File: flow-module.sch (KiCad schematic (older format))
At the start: 13 parts

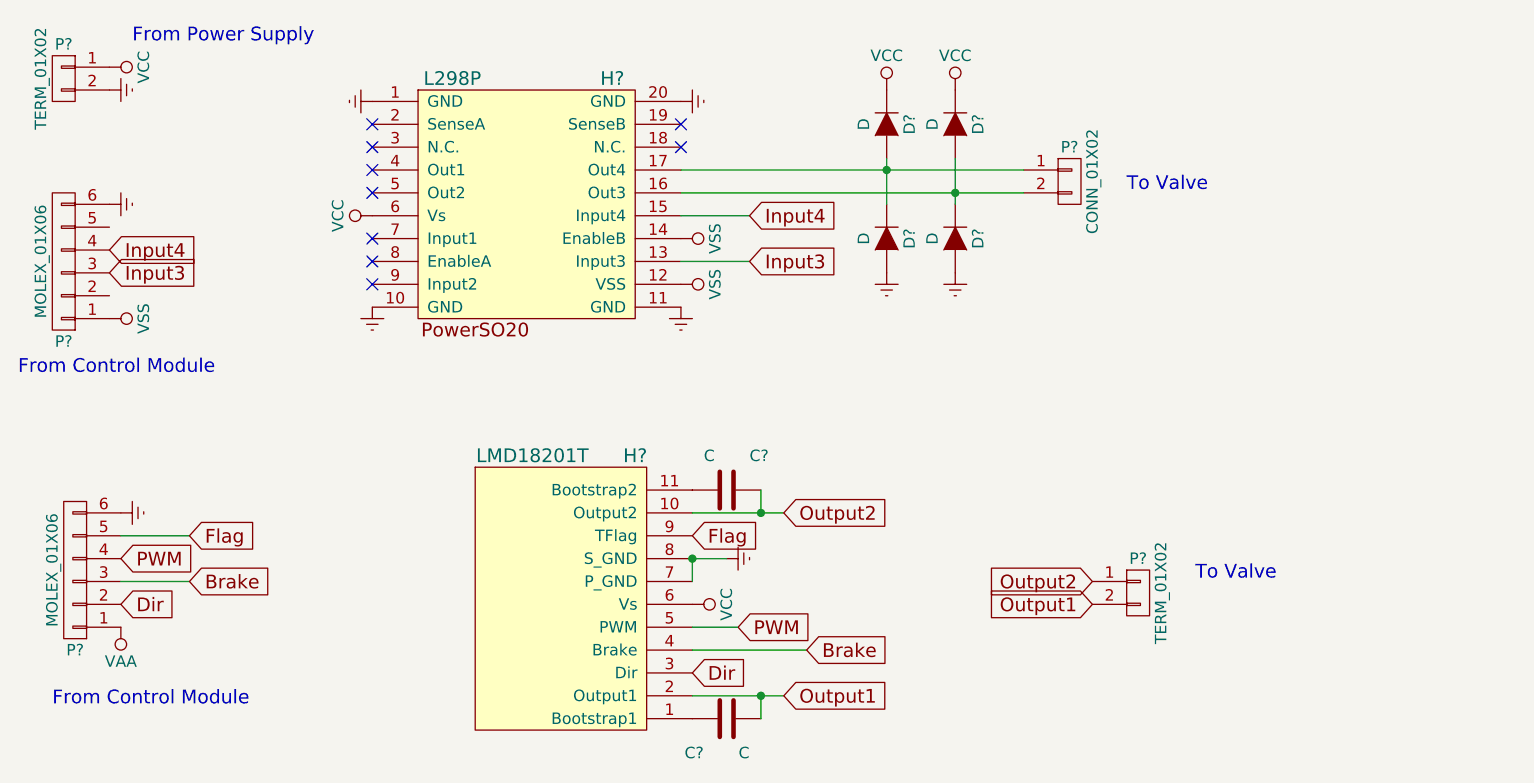
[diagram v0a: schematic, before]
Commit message: Added status LEDs to the schematic.
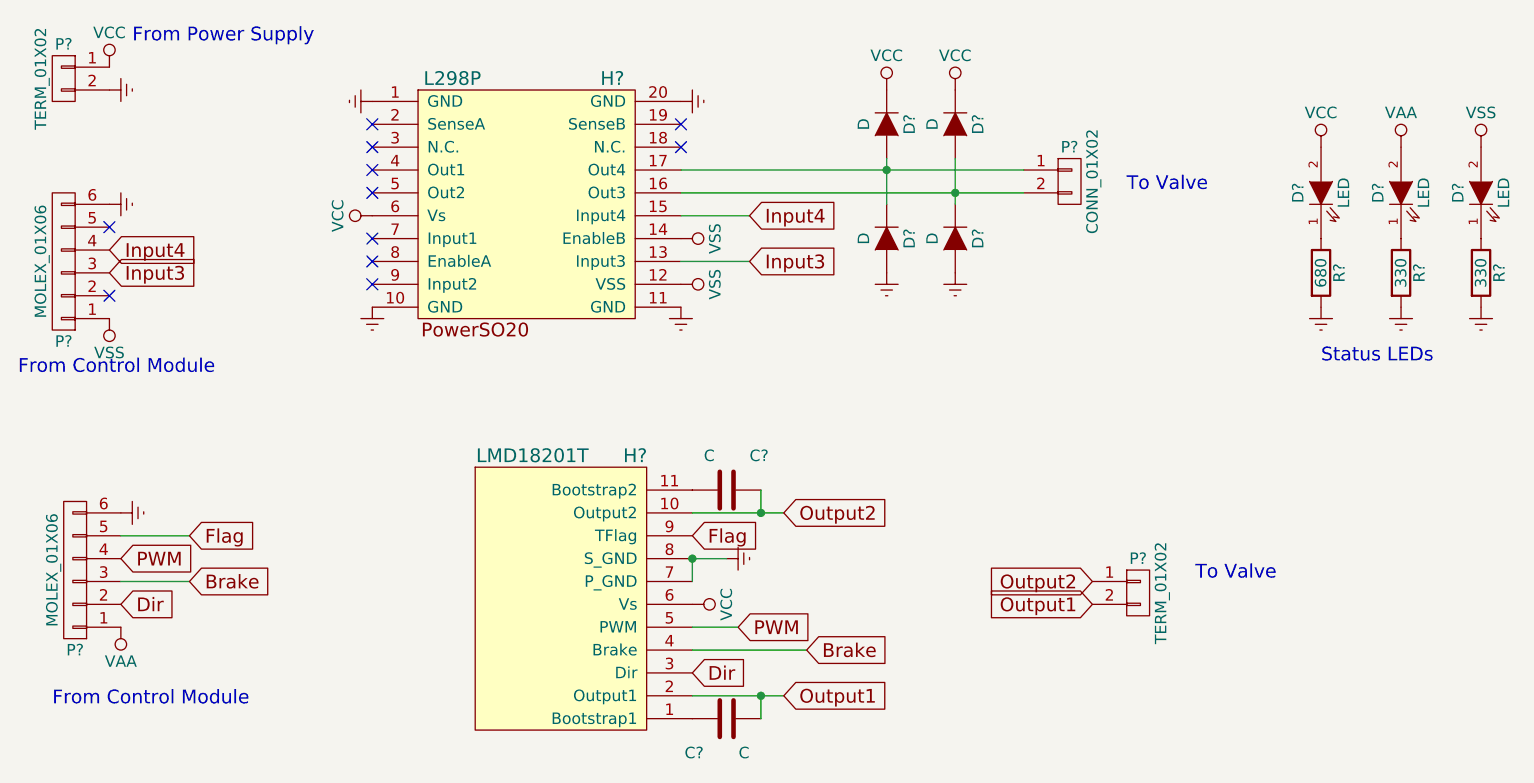
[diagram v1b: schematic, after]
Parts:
- added D? (x3): LED, symbol LED
- added R?: 680, symbol R
- added R? (x2): 330, symbol R
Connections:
- net Earth: now also R?.2, R?.2, R?.2
- net VAA: now also D?.2 (A)
- net VCC: now also D?.2 (A)
- net VSS: now also D?.2 (A)
- new net: D?.1 (K), R?.1 (x3)
- no-connect marks 9 -> 11
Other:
- note added: "Status LEDs\n"
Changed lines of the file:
@@
 LIBS:valves
 LIBS:valveteam
+LIBS:flow-module-cache
 EELAYER 25 0
 EELAYER END
@@
 F 3 "" H 1150 800 50  0000 C CNN
 	1    1150 800
-	0    1    1    0
+	1    0    0    -1
 $EndComp
 $Comp
@@
 F 3 "" H 1150 1900 50  0000 C CNN
 	1    1150 1900
-	0    1    1    0
+	-1   0    0    1
 $EndComp
 $Comp
@@
 Text Notes 900  3600 0    60   ~ 0
 From Control Module\n
+$Comp
+L VCC #PWR?
+U 1 1 5B052ACC
+P 6450 1150
+F 0 "#PWR?" H 6450 1000 50  0001 C CNN
+F 1 "VCC" H 6450 1300 50  0000 C CNN
+F 2 "" H 6450 1150 50  0000 C CNN
+F 3 "" H 6450 1150 50  0000 C CNN
+	1    6450 1150
+	1    0    0    -1
+$EndComp
+$Comp
+L VAA #PWR?
+U 1 1 5B052B8B
+P 6800 1150
+F 0 "#PWR?" H 6800 1000 50  0001 C CNN
+F 1 "VAA" H 6800 1300 50  0000 C CNN
+F 2 "" H 6800 1150 50  0000 C CNN
+F 3 "" H 6800 1150 50  0000 C CNN
+	1    6800 1150
+	1    0    0    -1
+$EndComp
+$Comp
+L VSS #PWR?
+U 1 1 5B052BBD
+P 7150 1150
+F 0 "#PWR?" H 7150 1000 50  0001 C CNN
+F 1 "VSS" H 7150 1300 50  0000 C CNN
+F 2 "" H 7150 1150 50  0000 C CNN
+F 3 "" H 7150 1150 50  0000 C CNN
+	1    7150 1150
+	1    0    0    -1
+$EndComp
+$Comp
+L LED D?
+U 1 1 5B052BE4
+P 6450 1350
+F 0 "D?" H 6450 1450 50  0000 C CNN
+F 1 "LED" H 6450 1250 50  0000 C CNN
+F 2 "" H 6450 1350 50  0000 C CNN
+F 3 "" H 6450 1350 50  0000 C CNN
+	1    6450 1350
+	0    -1   -1   0
+$EndComp
+$Comp
+L LED D?
+U 1 1 5B052C8D
+P 6800 1350
+F 0 "D?" H 6800 1450 50  0000 C CNN
+F 1 "LED" H 6800 1250 50  0000 C CNN
+F 2 "" H 6800 1350 50  0000 C CNN
+F 3 "" H 6800 1350 50  0000 C CNN
+	1    6800 1350
+	0    -1   -1   0
+$EndComp
+$Comp
+L LED D?
+U 1 1 5B052CD0
+P 7150 1350
+F 0 "D?" H 7150 1450 50  0000 C CNN
+F 1 "LED" H 7150 1250 50  0000 C CNN
+F 2 "" H 7150 1350 50  0000 C CNN
+F 3 "" H 7150 1350 50  0000 C CNN
+	1    7150 1350
+	0    -1   -1   0
+$EndComp
+$Comp
+L R R?
+U 1 1 5B052D3E
+P 6450 1700
+F 0 "R?" V 6530 1700 50  0000 C CNN
+F 1 "680" V 6450 1700 50  0000 C CNN
+F 2 "" V 6380 1700 50  0000 C CNN
+F 3 "" H 6450 1700 50  0000 C CNN
+	1    6450 1700
+	1    0    0    -1
+$EndComp
+$Comp
+L R R?
+U 1 1 5B052DC4
+P 6800 1700
+F 0 "R?" V 6880 1700 50  0000 C CNN
+F 1 "330" V 6800 1700 50  0000 C CNN
+F 2 "" V 6730 1700 50  0000 C CNN
+F 3 "" H 6800 1700 50  0000 C CNN
+	1    6800 1700
+	1    0    0    -1
+$EndComp
+$Comp
+L R R?
+U 1 1 5B052E1E
+P 7150 1700
+F 0 "R?" V 7230 1700 50  0000 C CNN
+F 1 "330" V 7150 1700 50  0000 C CNN
+F 2 "" V 7080 1700 50  0000 C CNN
+F 3 "" H 7150 1700 50  0000 C CNN
+	1    7150 1700
+	1    0    0    -1
+$EndComp
+$Comp
+L Earth #PWR?
+U 1 1 5B052E71
+P 6450 1850
+F 0 "#PWR?" H 6450 1600 50  0001 C CNN
+F 1 "Earth" H 6450 1700 50  0001 C CNN
+F 2 "" H 6450 1850 50  0000 C CNN
+F 3 "" H 6450 1850 50  0000 C CNN
+	1    6450 1850
+	1    0    0    -1
+$EndComp
+$Comp
+L Earth #PWR?
+U 1 1 5B052EB5
+P 6800 1850
+F 0 "#PWR?" H 6800 1600 50  0001 C CNN
+F 1 "Earth" H 6800 1700 50  0001 C CNN
+F 2 "" H 6800 1850 50  0000 C CNN
+F 3 "" H 6800 1850 50  0000 C CNN
+	1    6800 1850
+	1    0    0    -1
+$EndComp
+$Comp
+L Earth #PWR?
+U 1 1 5B052EF9
+P 7150 1850
+F 0 "#PWR?" H 7150 1600 50  0001 C CNN
+F 1 "Earth" H 7150 1700 50  0001 C CNN
+F 2 "" H 7150 1850 50  0000 C CNN
+F 3 "" H 7150 1850 50  0000 C CNN
+	1    7150 1850
+	1    0    0    -1
+$EndComp
+Text Notes 6450 2100 0    60   ~ 0
+Status LEDs\n
+NoConn ~ 1150 1500
+NoConn ~ 1150 1800
 $EndSCHEMATC

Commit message: Associate components and update the netlist.
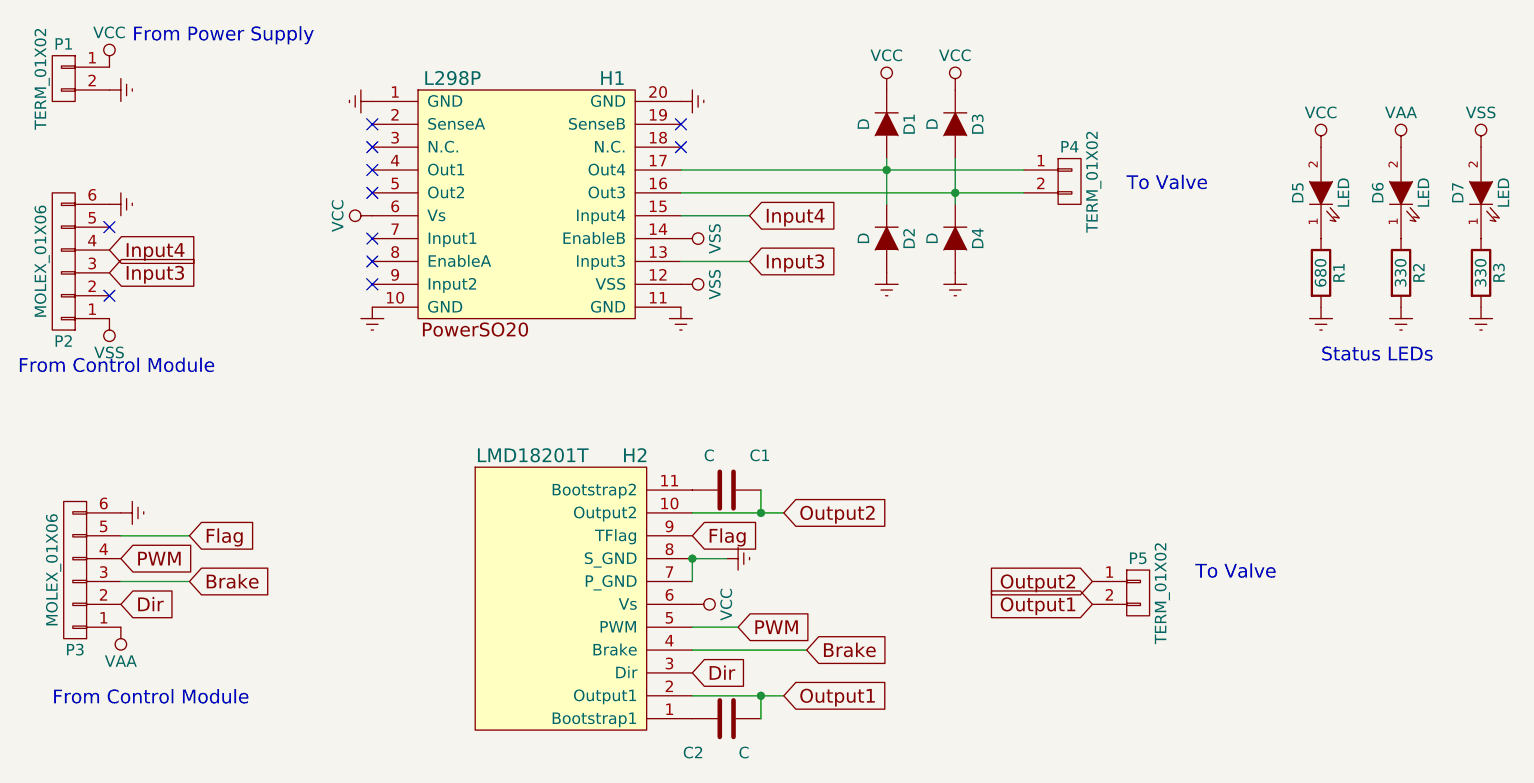
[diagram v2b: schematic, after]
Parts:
- removed P?: CONN_01X02, symbol CONN_01X02
- added P4: TERM_01X02, ValveTeam:TE_TERM, symbol CONN_01X02
- C1, C2: renamed from C?; footprint (none) -> Capacitors_SMD:C_0805_HandSoldering
- D1, D2, D3, D4: renamed from D?; footprint (none) -> ValveTeam:do219ab
- D5, D6, D7: renamed from D?; footprint (none) -> LEDs:LED_0805_HandSoldering
- H1: renamed from H?; footprint (none) -> ValveTeam:powerso-20
- H2: renamed from H?; footprint (none) -> ValveTeam:TO-220-11
- P1, P5: renamed from P?; footprint (none) -> ValveTeam:TE_TERM
- P2, P3: renamed from P?; footprint (none) -> ValveTeam:Molex_KK-6410-06_06x2.54mm_Straight
- R1, R2, R3: renamed from R?; footprint (none) -> Resistors_SMD:R_0805_HandSoldering
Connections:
- net at D1.2 (A), D2.1 (K), H1.17 (Out4): now also P4.1 (P1)
- net at D3.2 (A), D4.1 (K), H1.16 (Out3): now also P4.2 (P2)
